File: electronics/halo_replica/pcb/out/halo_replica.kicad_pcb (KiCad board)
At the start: 4 copper layers, 24.7 x 24.7 mm, 108 parts

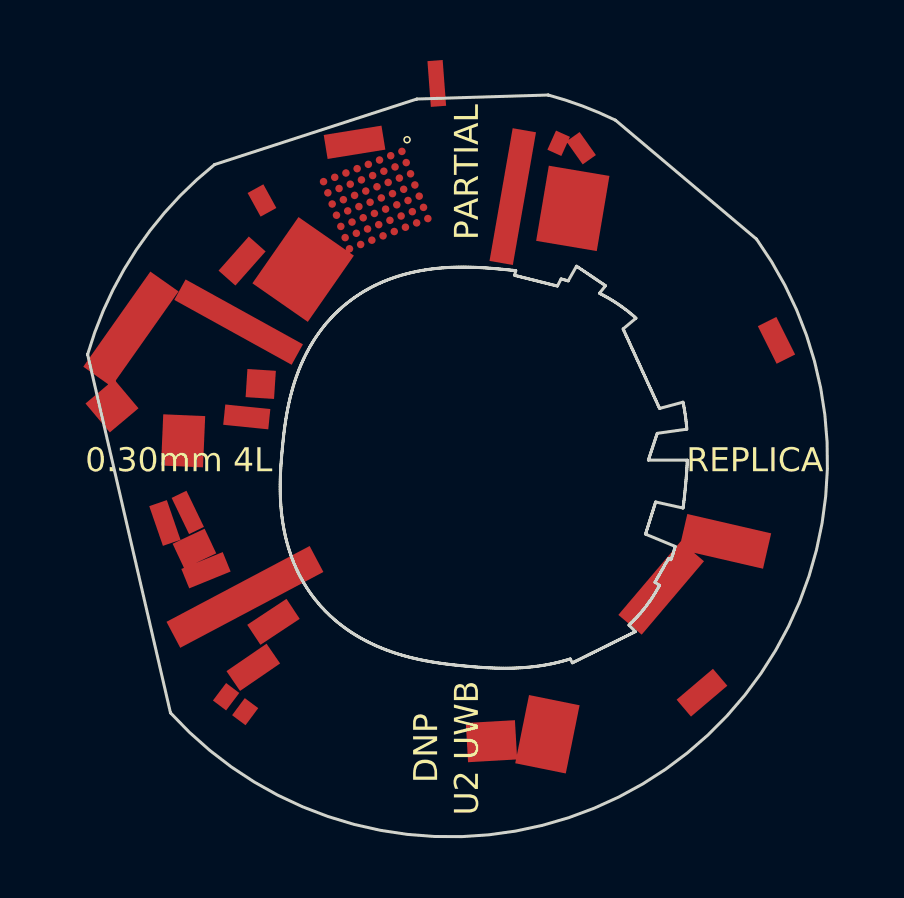
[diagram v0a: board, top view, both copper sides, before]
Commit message: L12: a .kicad_pcb that OPENS. Annular, routed pocket, 103 placements, DRC run
The Replica had no board file. It has one: pcb/out/halo_replica.kicad_pcb,
25.16 mm drawn OD, 4 layers, 0.30 mm, and it opens in KiCad 10.

THE EDGE IS FITTED PRIMITIVES, NOT A SILHOUETTE. Outer: 3 true arcs + 4
straight chords, endpoints solved exactly (circle-line quadratic, 2x2 for
line-line), never sampled. Pocket: superellipse n=2.4491 with 7 measured
straight facets and 14 radial step walls, 734 segments after dedupe, max
tessellation chord error 0.0322 mm against a 0.1029 mm registration floor.
The OD is a PARAMETER read from board.json, scaled by drawn/fitted; no
diameter is hard-coded anywhere in pcb/.

THE FAILURE THAT LOOKED LIKE NOTHING. The first build rendered a SQUARE
board. Two of the four admitted chords meet each other directly, and the
facet handovers landed on bearings where the facet radius already equalled
the superellipse's -- zero-length segments, 46 invalid_outline violations,
and KiCad silently FALLS BACK TO THE BOUNDING BOX. A malformed annulus and a
rectangle are the same picture until you look. Both are now deduped at 0.1 um
and the chain closure is CHECKED, not assumed.

PLACED, all 100 handoff rows, every flag obeyed:
  31 CLASS B measured metal lands, real F.Cu, at the MEASURED long-side
     bearing (rot = 90 - angle, keyed on position not row order; the handoff
     drops the angle and the producing files keep it)
  52 position-only, 14 rim-material-suspect, 3 do_not_draw, 3 eyeballed
     absences -- all NO COPPER, the refusal in the value field
   5 dark bodies named as ABSENT and nothing drawn there

THE COPPER I REFUSED, ON L11'S WARNING. U1's WLCSP-50 land pattern is NOT
landed. A 0.40 mm grid in the measured 3.226 x 2.956 mm body is 56 positions
for 50 balls and no ball map exists here or in KiCad's 179 Package_CSP
footprints. Six lands that do not exist on the part are six lands a fab would
make. Body and grid go on F.Fab only; the solderable versio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
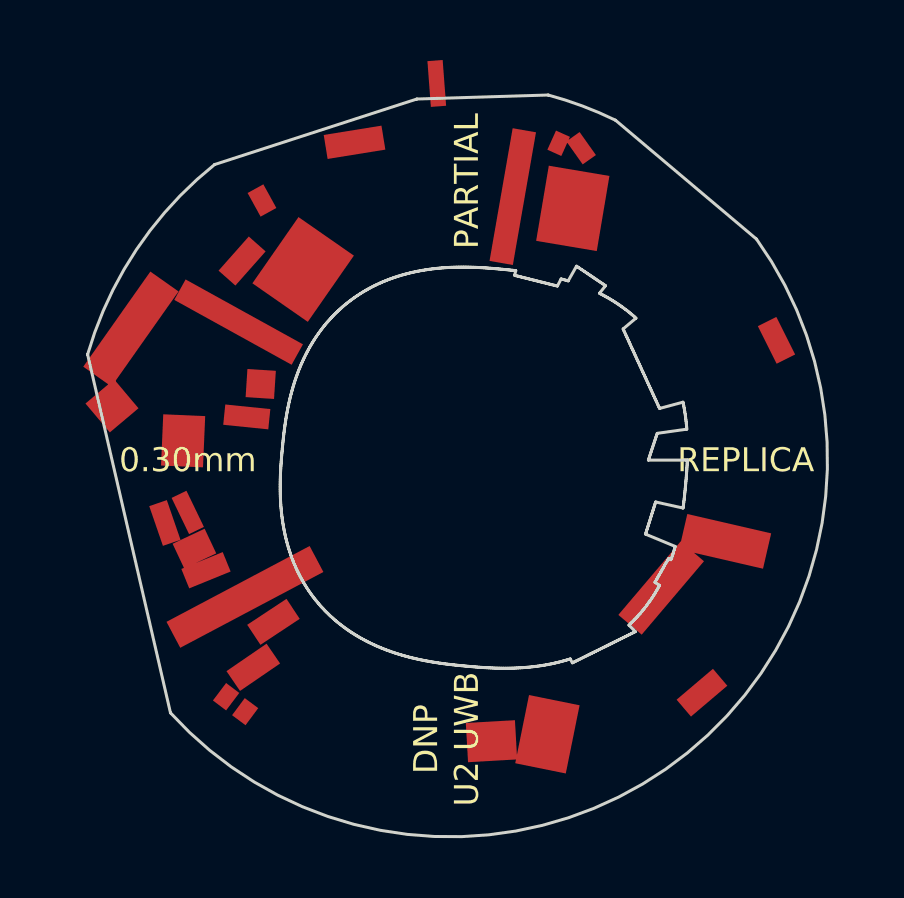
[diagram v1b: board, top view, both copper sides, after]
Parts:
- D000: value U1 nRF52832-CIAA WLCSP-50 - 56 LANDS DRAWN, 6 UNKNOWN; A1 CORNER CANNOT DETERMINE; body measured 3.28x3.03 mm here -> U1 nRF52832-CIAA WLCSP-50 - NO LANDS DRAWN. Ball map CANNOT DETERMINE; body measured 3.28x3.03 mm; A1 corner unknown; footprint REPL_WLCSP_8x7_P0.4_GRID56 -> REPL_U1_WLCSP50_NO_LANDS
- moved SILK1 0.30 mm to (24.3, 12.2)
- moved SILK2 0.30 mm to (15.0, 21.5)
- moved SILK4 0.30 mm to (15.0, 2.87)
- moved SILK3 0.30 mm to (5.70, 12.2)

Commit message: L9: the fourth column - a report's row state and its contents are different facts
D6 showed "valid=yes", which by this file's own rules means ITS SOURCE (the ERC) was
clean - and reads to anyone scanning a table for green as "the DRC passed". IT DID NOT:
the Replica's DRC reports 42 errors against 3 warnings, with actual clearances down to
0.0000 mm. Documenting that trap was the weaker option. The column that says so is now
beside it, and the third column is renamed from "valid" to "source ok", because "valid"
is the word that invited the misreading.

  opens | current | source ok | ITS OWN VERDICT

D6 now prints ** 42E 0U ** with: "THIS ROW IS GREEN AS AN ARTIFACT AND THE THING IT
GRADES IS NOT. Anything cut from that source fails the third leg."

A FAILING REPORT DOES NOT TURN ITS OWN ROW RED, and that is deliberate. The artifact is
not the defect. Turning D6 red on its contents would conflate "we have no DRC" with "the
DRC found things", which is the could-not-build / could-not-verify conflation this
project has a standing rule against. Contents gate the things that DEPEND on them, which
is exactly what the third leg already does for D7 and D8.

Two more breaks, 13 deliverable breaks total, all watched:
  W-1  a CLEAN DRC          -> 0E 0U, clean
  W-2  2 errors, 1 warning  -> 2E 0U flagged, ROW STILL GREEN
W-2's fixture needed an ERC added before it could test anything: without one the row is
CANNOT DETERMINE and the claim W-2 makes cannot be reached. A break whose fixture cannot
reach the state under test is not a break. THIRD TIME TODAY a break asserted past the
property it was written for.

AND E08 NOW OPENS WITH THE SENTENCE THAT EXPLAINS THE WHOLE LANE, since E07 is closed at
32 and this is a sentence about all of them rather than a thirty-third:

  THE LESSON IS NOT INSTALLED BY WRITING IT DOWN. IT IS INSTALLED BY HAVING A MECHANISM
  THAT RE-RUNS IT AGAINST NEW GROUND.

Five controls here passed today without being able to fail, each checking something
A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
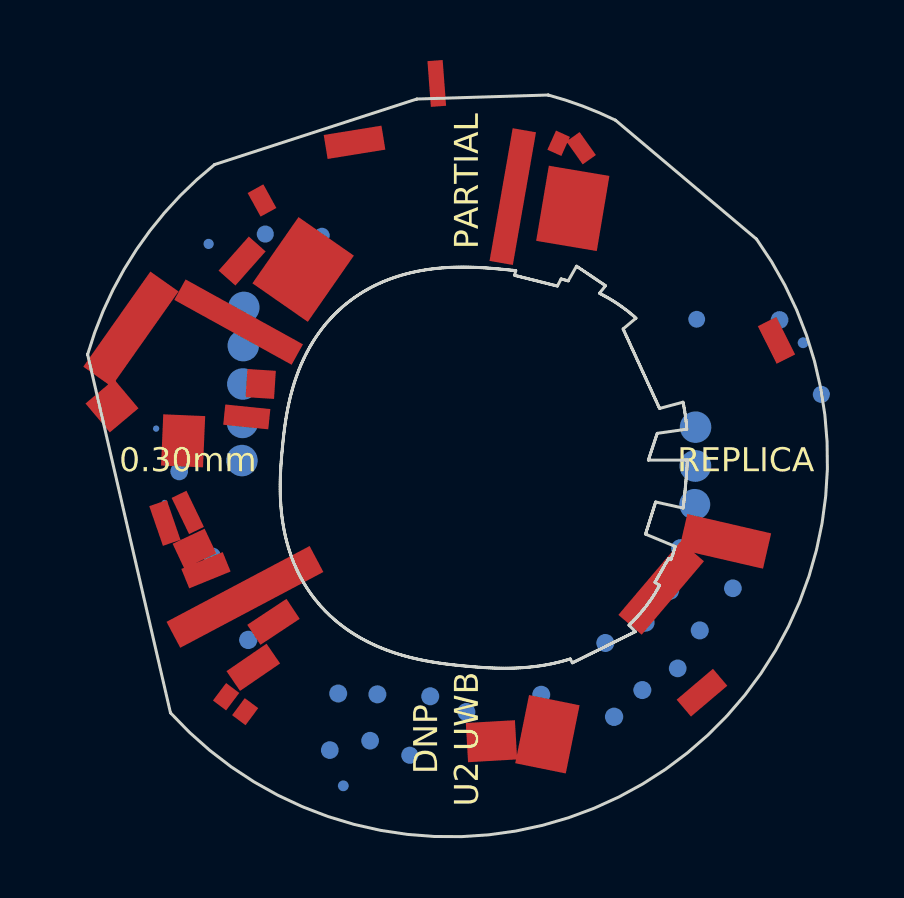
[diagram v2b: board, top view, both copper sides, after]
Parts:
- added KC000: BATTERY CONTACT - POSITION ONLY; the 1.495 mm extent is NOT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, REPL_BACK_CONTACT_POS, B.Cu at (17.7, 4.32)
- added KC001: BATTERY CONTACT - POSITION ONLY; the 3.321 mm extent is NOT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, REPL_BACK_CONTACT_POS, B.Cu at (15.1, 3.61)
- added KC002: BATTERY CONTACT - POSITION ONLY; the 1.682 mm extent is NOT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, REPL_BACK_CONTACT_POS, B.Cu at (12.6, 4.25)
- added KP000: MEASURED GOLD PAD d=1.05 mm (equivalent circle) conf=medium, REPL_BPAD_D1.05, B.Cu at (22.6, 11.1)
- added KP001: MEASURED GOLD PAD d=0.57 mm (equivalent circle) conf=high, REPL_BPAD_D0.57, B.Cu at (26.8, 9.98)
- added KP002: MEASURED GOLD PAD d=0.36 mm (equivalent circle) conf=medium, REPL_BPAD_D0.36, B.Cu at (26.2, 8.26)
- added KP003: MEASURED GOLD PAD d=0.59 mm (equivalent circle) conf=high, REPL_BPAD_D0.59, B.Cu at (25.4, 7.50)
- added KP004: MEASURED GOLD PAD d=0.56 mm (equivalent circle) conf=high, REPL_BPAD_D0.56, B.Cu at (22.7, 7.47)
- added KP007: MEASURED GOLD PAD d=0.52 mm (equivalent circle) conf=high, REPL_BPAD_D0.52, B.Cu at (10.2, 4.68)
- added KP008: MEASURED GOLD PAD d=0.57 mm (equivalent circle) conf=high, REPL_BPAD_D0.57, B.Cu at (8.28, 4.63)
- added KP009: MEASURED GOLD PAD d=0.34 mm (equivalent circle) conf=medium, REPL_BPAD_D0.34, B.Cu at (6.39, 4.96)
- added KP010: MEASURED GOLD PAD d=1.05 mm (equivalent circle) conf=medium, REPL_BPAD_D1.05, B.Cu at (7.57, 7.08)
- added KP011: MEASURED GOLD PAD d=1.05 mm (equivalent circle) conf=medium, REPL_BPAD_D1.05, B.Cu at (7.55, 8.35)
- added KP012: MEASURED GOLD PAD d=1.05 mm (equivalent circle) conf=medium, REPL_BPAD_D1.05, B.Cu at (7.54, 9.63)
- added KP013: MEASURED GOLD PAD d=1.05 mm (equivalent circle) conf=medium, REPL_BPAD_D1.05, B.Cu at (7.52, 10.9)
- added KP014: MEASURED GOLD PAD d=0.21 mm (equivalent circle) conf=medium, REPL_BPAD_D0.21, B.Cu at (4.64, 11.1)
- added KP015: MEASURED GOLD PAD d=0.6 mm (equivalent circle) conf=high, REPL_BPAD_D0.6, B.Cu at (5.43, 11.4)
- added KP016: MEASURED GOLD PAD d=1.05 mm (equivalent circle) conf=medium, REPL_BPAD_D1.05, B.Cu at (7.50, 12.2)
- added KP017: MEASURED GOLD PAD d=0.59 mm (equivalent circle) conf=high, REPL_BPAD_D0.59, B.Cu at (5.41, 12.5)
- added KP018: MEASURED GOLD PAD d=0.21 mm (equivalent circle) conf=medium, REPL_BPAD_D0.21, B.Cu at (4.93, 13.6)
- added KP019: MEASURED GOLD PAD d=0.6 mm (equivalent circle) conf=high, REPL_BPAD_D0.6, B.Cu at (6.51, 15.4)
- added KP020: MEASURED GOLD PAD d=0.6 mm (equivalent circle) conf=high, REPL_BPAD_D0.6, B.Cu at (6.90, 17.1)
- added KP021: MEASURED GOLD PAD d=0.61 mm (equivalent circle) conf=high, REPL_BPAD_D0.61, B.Cu at (7.72, 18.2)
- added KP022: MEASURED GOLD PAD d=0.6 mm (equivalent circle) conf=high, REPL_BPAD_D0.6, B.Cu at (10.7, 19.9)
- added KP023: MEASURED GOLD PAD d=0.59 mm (equivalent circle) conf=high, REPL_BPAD_D0.59, B.Cu at (10.4, 21.8)
- added KP024: MEASURED GOLD PAD d=0.6 mm (equivalent circle) conf=high, REPL_BPAD_D0.6, B.Cu at (12.0, 20.0)
- added KP025: MEASURED GOLD PAD d=0.36 mm (equivalent circle) conf=medium, REPL_BPAD_D0.36, B.Cu at (10.9, 23.0)
- added KP026: MEASURED GOLD PAD d=0.59 mm (equivalent circle) conf=high, REPL_BPAD_D0.59, B.Cu at (11.8, 21.5)
- added KP027: MEASURED GOLD PAD d=0.57 mm (equivalent circle) conf=high, REPL_BPAD_D0.57, B.Cu at (13.1, 22.0)
- added KP028: MEASURED GOLD PAD d=0.6 mm (equivalent circle) conf=high, REPL_BPAD_D0.6, B.Cu at (13.8, 20.0)
- added KP029: MEASURED GOLD PAD d=0.6 mm (equivalent circle) conf=high, REPL_BPAD_D0.6, B.Cu at (15.0, 20.6)
- added KP030: MEASURED GOLD PAD d=0.6 mm (equivalent circle) conf=high, REPL_BPAD_D0.6, B.Cu at (17.5, 20.0)
- added KP031: MEASURED GOLD PAD d=0.61 mm (equivalent circle) conf=high, REPL_BPAD_D0.61, B.Cu at (19.9, 20.7)
- added KP032: MEASURED GOLD PAD d=0.6 mm (equivalent circle) conf=high, REPL_BPAD_D0.6, B.Cu at (19.6, 18.3)
- added KP033: MEASURED GOLD PAD d=0.6 mm (equivalent circle) conf=high, REPL_BPAD_D0.6, B.Cu at (20.9, 19.8)
- added KP034: MEASURED GOLD PAD d=0.59 mm (equivalent circle) conf=high, REPL_BPAD_D0.59, B.Cu at (22.0, 19.1)
- added KP035: MEASURED GOLD PAD d=0.6 mm (equivalent circle) conf=high, REPL_BPAD_D0.6, B.Cu at (21.0, 17.6)
- added KP036: MEASURED GOLD PAD d=0.6 mm (equivalent circle) conf=high, REPL_BPAD_D0.6, B.Cu at (22.8, 17.8)
- added KP037: MEASURED GOLD PAD d=0.61 mm (equivalent circle) conf=high, REPL_BPAD_D0.61, B.Cu at (21.8, 16.5)
- added KP038: MEASURED GOLD PAD d=0.59 mm (equivalent circle) conf=high, REPL_BPAD_D0.59, B.Cu at (23.9, 16.4)
- added KP039: MEASURED GOLD PAD d=0.62 mm (equivalent circle) conf=high, REPL_BPAD_D0.62, B.Cu at (22.1, 15.1)
- added KP040: MEASURED GOLD PAD d=0.61 mm (equivalent circle) conf=high, REPL_BPAD_D0.61, B.Cu at (23.5, 15.1)
- added KP041: MEASURED GOLD PAD d=1.03 mm (equivalent circle) conf=medium, REPL_BPAD_D1.03, B.Cu at (22.6, 13.6)
- added KP042: MEASURED GOLD PAD d=1.06 mm (equivalent circle) conf=medium, REPL_BPAD_D1.06, B.Cu at (22.6, 12.4)
